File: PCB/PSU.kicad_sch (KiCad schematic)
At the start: 47 parts, among them Q2 BSS138BKS, U12 TPS61040DBV, U13 INA180A4, U14 TPS259533, U6 AP2127K-ADJ, U7 AMS1117-3.3, U9 TPS259533

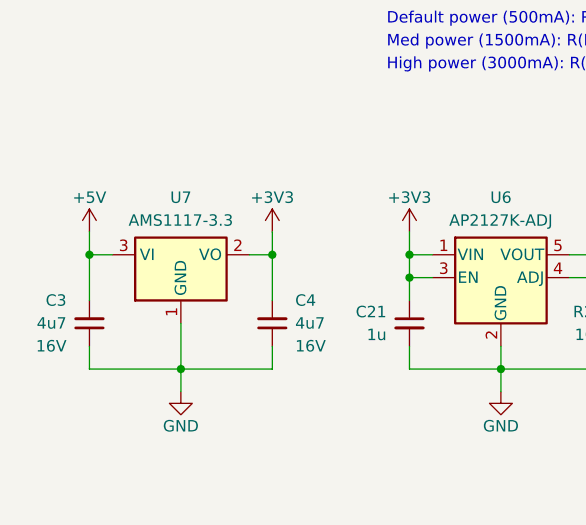
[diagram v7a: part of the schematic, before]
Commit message: Improved switch footprints and changed LDO.
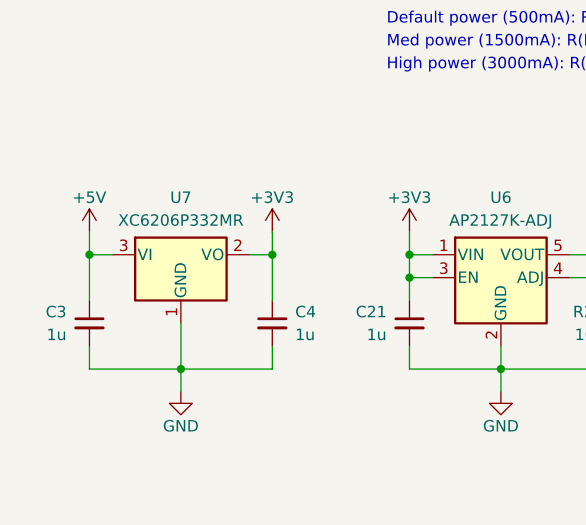
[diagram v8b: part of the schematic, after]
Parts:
- removed U7: AMS1117-3.3, Package_TO_SOT_SMD:SOT-223-3_TabPin2, symbol Regulator_Linear:AMS1117-3.3
- added U7: XC6206P332MR, Honeydew:SOT-23-3, symbol Regulator_Linear:XC6206PxxxMR
- C3, C4: value 4u7 -> 1u; LCSC C19666 -> C15849; Voltage 16V -> 50V
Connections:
- net +3V3: now also C4.1, U7.2 (VO); no longer C4.2
- net +5V: now also C3.1, U7.3 (VI); no longer C3.2
- net GND: now also C3.2, C4.2, U7.1 (GND); no longer C3.1, C4.1
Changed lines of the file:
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@@
+    )
+  )
+  (symbol (lib_id "Device:C_Small") (at 22.86 134.62 0) (unit 1)
+    (in_bom yes) (on_board yes) (dnp no) (fields_autoplaced)
+    (property "Reference" "C3" (at 20.32 133.3562 0)
+      (effects (font (size 1.27 1.27)) (justify right))
+    )
+    (property "Value" "1u" (at 20.32 135.8962 0)
+      (effects (font (size 1.27 1.27)) (justify right))
+    )
+    (property "Footprint" "Capacitor_SMD:C_0603_1608Metric" (at 22.86 134.62 0)
+      (effects (font (size 1.27 1.27)) hide)
+    )
+    (property "Datasheet" "" (at 22.86 134.62 0)
+      (effects (font (size 1.27 1.27)) hide)
+    )
+    (property "Description" "0603 capacitor" (at 22.86 134.62 0)
+      (effects (font (size 1.27 1.27)) hide)
+    )
+    (property "LCSC" "C15849" (at 22.86 134.62 0)
+      (effects (font (size 1.27 1.27)) hide)
+    )
+    (property "Voltage" "50V" (at 22.86 134.62 0)
+      (effects (font (size 1.27 1.27)) hide)
+    )
+    (pin "1")
+    (pin "2")
+    (instances
+      (project "Honeydew"
+        (path "/534caec7-cf60-4f90-b1ed-42c9d445ef0f/0e23afb1-1d24-49d7-b6b4-dea31b732359"
+          (reference "C3") (unit 1)
+        )
+      )
     )
   )
@@
     )
   )
-  (symbol (lib_id "Regulator_Linear:AMS1117-3.3") (at 33.02 127 0) (unit 1)
-    (in_bom yes) (on_board yes) (dnp no) (fields_autoplaced)
-    (property "Reference" "U7" (at 33.02 120.65 0)
-      (effects (font (size 1.27 1.27)))
-    )
-    (property "Value" "AMS1117-3.3" (at 33.02 123.19 0)
-      (effects (font (size 1.27 1.27)))
-    )
-    (property "Footprint" "Package_TO_SOT_SMD:SOT-223-3_TabPin2" (at 33.02 121.92 0)
-      (effects (font (size 1.27 1.27)) hide)
-    )
-    (property "Datasheet" "http://www.advanced-monolithic.com/pdf/ds1117.pdf" (at 35.56 133.35 0)
-      (effects (font (size 1.27 1.27)) hide)
-    )
-    (property "Description" "3.3V Regulator" (at 33.02 127 0)
-      (effects (font (size 1.27 1.27)) hide)
-    )
-    (property "LCSC" "C6186" (at 33.02 127 0)
-      (effects (font (size 1.27 1.27)) hide)
-    )
-    (pin "1")
-    (pin "2")
-    (pin "3")
-    (instances
-      (project "Honeydew"
-        (path "/534caec7-cf60-4f90-b1ed-42c9d445ef0f/0e23afb1-1d24-49d7-b6b4-dea31b732359"
-          (reference "U7") (unit 1)
-        )
-      )
-    )
-  )
-  (symbol (lib_id "Device:C_Small") (at 43.18 134.62 0) (mirror x) (unit 1)
-    (in_bom yes) (on_board yes) (dnp no)
-    (property "Reference" "C4" (at 45.72 132.08 0)
-      (effects (font (size 1.27 1.27)) (justify left))
-    )
-    (property "Value" "4u7" (at 45.72 134.62 0)
-      (effects (font (size 1.27 1.27)) (justify left))
-    )
-    (property "Footprint" "Capacitor_SMD:C_0603_1608Metric" (at 43.18 134.62 0)
-      (effects (font (size 1.27 1.27)) hide)
-    )
-    (property "Datasheet" "" (at 43.18 134.62 0)
-      (effects (font (size 1.27 1.27)) hide)
-    )
-    (property "Description" "0603 capacitor" (at 43.18 134.62 0)
-      (effects (font (size 1.27 1.27)) hide)
-    )
-    (property "LCSC" "C19666" (at 43.18 134.62 0)
-      (effects (font (size 1.27 1.27)) hide)
-    )
-    (property "Voltage" "16V" (at 45.72 137.16 0)
-      (effects (font (size 1.27 1.27)) (justify left))
-    )
-    (pin "1")
-    (pin "2")
-    (instances
-      (project "Honeydew"
-        (path "/534caec7-cf60-4f90-b1ed-42c9d445ef0f/0e23afb1-1d24-49d7-b6b4-dea31b732359"
-          (reference "C4") (unit 1)
-        )
-      )
-    )
-  )
   (symbol (lib_id "Device:R_Small") (at 109.22 63.5 180) (unit 1)
     (in_bom yes) (on_board yes) (dnp no)
@@
         (path "/534caec7-cf60-4f90-b1ed-42c9d445ef0f/0e23afb1-1d24-49d7-b6b4-dea31b732359"
           (reference "R18") (unit 1)
+        )
+      )
+    )
+  )
+  (symbol (lib_id "Regulator_Linear:XC6206PxxxMR") (at 33.02 127 0) (unit 1)
+    (in_bom yes) (on_board yes) (dnp no) (fields_autoplaced)
+    (property "Reference" "U7" (at 33.02 120.65 0)
+      (effects (font (size 1.27 1.27)))
+    )
+    (property "Value" "XC6206P332MR" (at 33.02 123.19 0)
+      (effects (font (size 1.27 1.27)))
+    )
+    (property "Footprint" "Honeydew:SOT-23-3" (at 33.02 121.285 0)
+      (effects (font (size 1.27 1.27) italic) hide)
+    )
+    (property "Datasheet" "https://www.torexsemi.com/file/xc6206/XC6206.pdf" (at 33.02 127 0)
+      (effects (font (size 1.27 1.27)) hide)
+    )
+    (property "LCSC" "C5446" (at 33.02 127 0)
+      (effects (font (size 1.27 1.27)) hide)
+    )
+    (pin "1")
+    (pin "2")
+    (pin "3")
+    (instances
+      (project "Honeydew"
+        (path "/534caec7-cf60-4f90-b1ed-42c9d445ef0f/0e23afb1-1d24-49d7-b6b4-dea31b732359"
+          (reference "U7") (unit 1)
         )
       )
@@
     )
   )
-  (symbol (lib_id "Device:C_Small") (at 22.86 134.62 180) (unit 1)
-    (in_bom yes) (on_board yes) (dnp no)
-    (property "Reference" "C3" (at 20.32 132.08 0)
-      (effects (font (size 1.27 1.27)) (justify left))
-    )
-    (property "Value" "4u7" (at 20.32 134.62 0)
-      (effects (font (size 1.27 1.27)) (justify left))
-    )
-    (property "Footprint" "Capacitor_SMD:C_0603_1608Metric" (at 22.86 134.62 0)
-      (effects (font (size 1.27 1.27)) hide)
-    )
-    (property "Datasheet" "" (at 22.86 134.62 0)
-      (effects (font (size 1.27 1.27)) hide)
-    )
-    (property "Description" "0603 capacitor" (at 22.86 134.62 0)
-      (effects (font (size 1.27 1.27)) hide)
-    )
-    (property "LCSC" "C19666" (at 22.86 134.62 0)
-      (effects (font (size 1.27 1.27)) hide)
-    )
-    (property "Voltage" "16V" (at 20.32 137.16 0)
-      (effects (font (size 1.27 1.27)) (justify left))
-    )
-    (pin "1")
-    (pin "2")
-    (instances
-      (project "Honeydew"
-        (path "/534caec7-cf60-4f90-b1ed-42c9d445ef0f/0e23afb1-1d24-49d7-b6b4-dea31b732359"
-          (reference "C3") (unit 1)
-        )
-      )
-    )
-  )
   (symbol (lib_id "Device:D_Small") (at 132.08 127 180) (unit 1)
     (in_bom yes) (on_board yes) (dnp no) (fields_autoplaced)
@@
         )
       )
+    )
+  )
+  (symbol (lib_id "Device:C_Small") (at 43.18 134.62 0) (mirror y) (unit 1)
+    (in_bom yes) (on_board yes) (dnp no)
+    (property "Reference" "C4" (at 45.72 133.3562 0)
+      (effects (font (size 1.27 1.27)) (justify right))
+    )
+    (property "Value" "1u" (at 45.72 135.8962 0)
+      (effects (font (size 1.27 1.27)) (justify right))
+    )
+    (property "Footprint" "Capacitor_SMD:C_0603_1608Metric" (at 43.18 134.62 0)
+      (effects (font (size 1.27 1.27)) hide)
+    )
+    (property "Datasheet" "" (at 43.18 134.62 0)
+      (effects (font (size 1.27 1.27)) hide)
+    )
+    (property "Description" "0603 capacitor" (at 43.18 134.62 0)
+      (effects (font (size 1.27 1.27)) hide)
+    )
+    (property "LCSC" "C15849" (at 43.18 134.62 0)
+      (effects (font (size 1.27 1.27)) hide)
+    )
+    (property "Voltage" "50V" (at 43.18 134.62 0)
+      (effects (font (size 1.27 1.27)) hide)
+    )
+    (pin "1")
+    (pin "2")
+    (instances
+      (project "Honeydew"
+        (path "/534caec7-cf60-4f90-b1ed-42c9d445ef0f/0e23afb1-1d24-49d7-b6b4-dea31b732359"
+          (reference "C4") (unit 1)
+        )
+      )
